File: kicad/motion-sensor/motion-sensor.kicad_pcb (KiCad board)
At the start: 2 copper layers, 53.7 x 28.7 mm, 0 parts

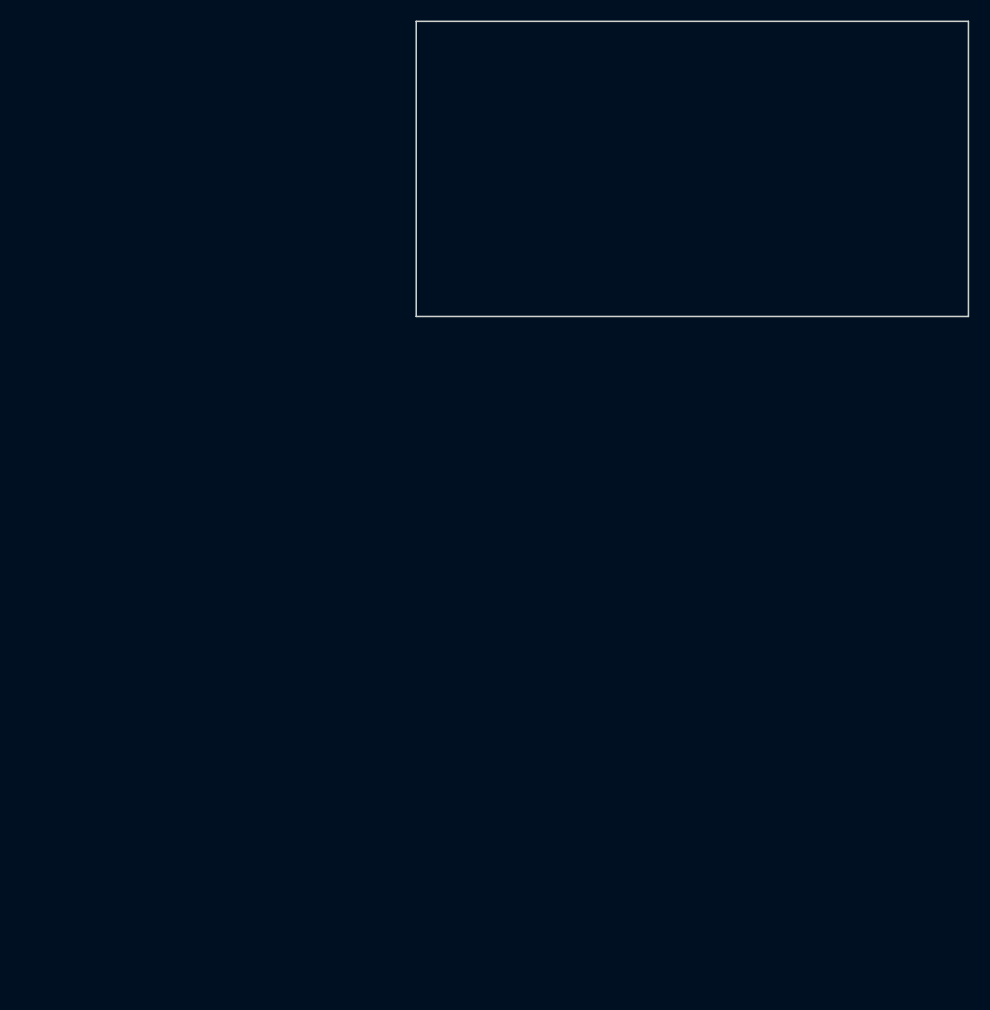
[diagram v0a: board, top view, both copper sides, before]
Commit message: motion sensor project in kicad
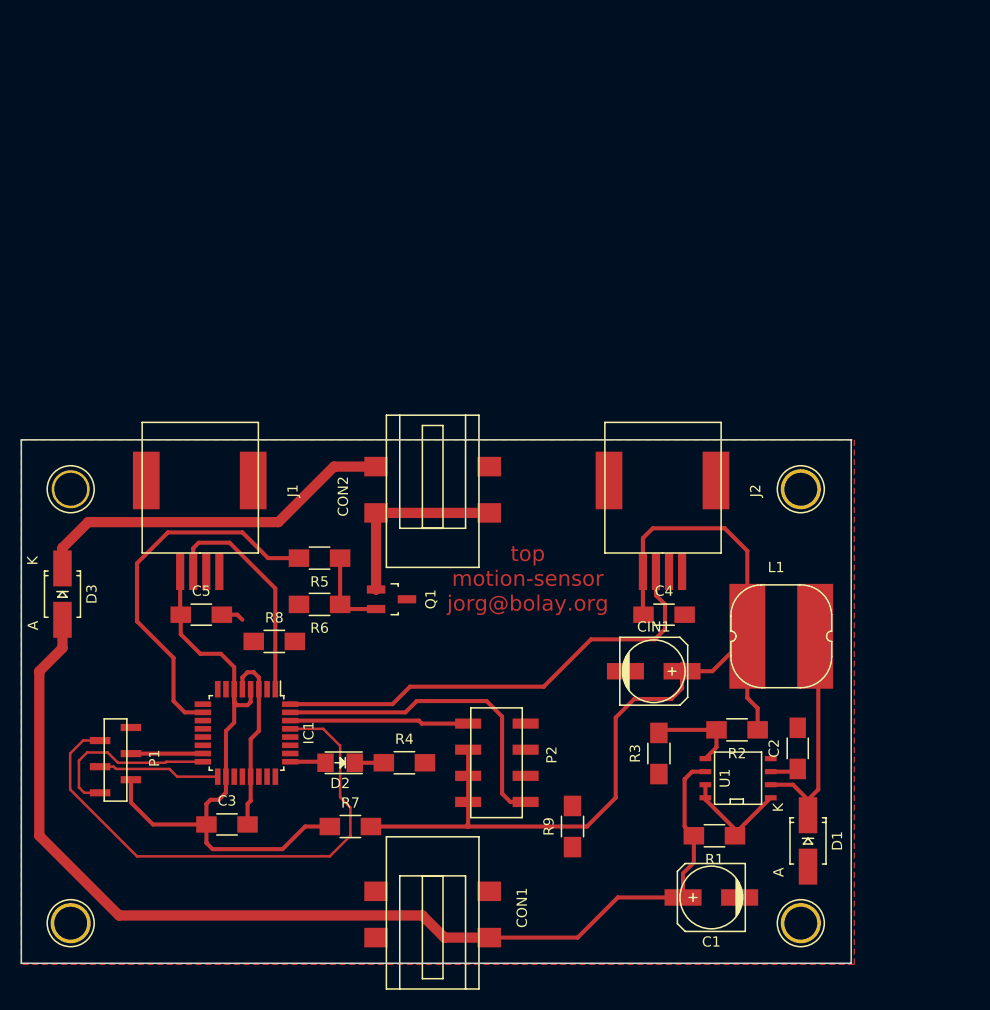
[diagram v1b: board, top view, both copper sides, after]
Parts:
- added C1: 100uF, Capacitors_SMD:c_elec_6.3x7.7, F.Cu at (117.1, 144.5)
- added C2: 160pF, Capacitors_SMD:C_1206_HandSoldering, F.Cu at (125.5, 130.0)
- added C3: 100nF, Capacitors_SMD:C_1206_HandSoldering, F.Cu at (70.0, 137.4)
- added C4: 100nF, Capacitors_SMD:C_1206_HandSoldering, F.Cu at (112.5, 117.0)
- added C5: 100nF, Capacitors_SMD:C_1206_HandSoldering, F.Cu at (67.5, 117.0)
- added CIN1: 50uF, Capacitors_SMD:c_elec_6.3x7.7, F.Cu at (111.5, 122.5)
- added CON1: LUM 1613-14, bolay library:barrel_jack_ds_1613_14, F.Cu at (90.0, 146.0)
- added CON2: LUM 1613-14, bolay library:barrel_jack_ds_1613_14, F.Cu at (90.0, 105.0)
- added D1: B140F, Diodes_SMD:SMA_Handsoldering, F.Cu at (126.5, 139.0)
- added D2: LED, LEDs:LED_1206, F.Cu at (81.0, 131.4)
- added D3: B140F, Diodes_SMD:SMA_Handsoldering, F.Cu at (54.0, 115.0)
- added IC1: ATMEGA328P-A AU 1537, Housings_QFP:TQFP-32_7x7mm_Pitch0.8mm, F.Cu at (71.9, 128.5)
- added J1: RJ10_4p4c, bolay library:RJ10_SMD_4p4c, F.Cu at (61.0, 111.0)
- added J2: RJ10_4p4c, bolay library:RJ10_SMD_4p4c, F.Cu at (106.0, 111.0)
- added L1: 35uH, bolay library:SRN_1060_Power_Inductors, F.Cu at (123.9, 119.1)
- added P1: ISP, bolay library:6x1pin_50mil_header, F.Cu at (59.4, 131.2)
- added P2: ESP8266, bolay library:8pin_Header_SMD, F.Cu at (96.5, 131.4)
- added Q1: FDN337N, TO_SOT_Packages_SMD:SOT-23_Handsoldering, F.Cu at (86.0, 115.5)
- added R1: 0.33, Resistors_SMD:R_1206_HandSoldering, F.Cu at (117.4, 138.5)
- added R2: 18k, Resistors_SMD:R_1206_HandSoldering, F.Cu at (119.6, 128.2)
- added R3: 11k, Resistors_SMD:R_1206_HandSoldering, F.Cu at (112.0, 130.5)
- added R4: 560, Resistors_SMD:R_1206_HandSoldering, F.Cu at (87.2, 131.4)
- added R5: 1K, Resistors_SMD:R_1206_HandSoldering, F.Cu at (79.0, 111.5)
- added R6: 1M, Resistors_SMD:R_1206_HandSoldering, F.Cu at (79.0, 116.0)
- added R7: 0, Resistors_SMD:R_1206_HandSoldering, F.Cu at (82.0, 137.6)
- added R8: 0, Resistors_SMD:R_1206_HandSoldering, F.Cu at (74.6, 119.6)
- added R9: 0, Resistors_SMD:R_1206_HandSoldering, F.Cu at (103.6, 137.6)
- added REF**: 1pin, Connect:1pin, F.Cu at (125.8, 104.8)
- added REF**: 1pin, Connect:1pin, F.Cu at (125.8, 147.0)
- added REF**: 1pin, Connect:1pin, F.Cu at (54.8, 104.8)
- added REF**: 1pin, Connect:1pin, F.Cu at (54.8, 147.0)
- added U1: MC34063, SMD_Packages:SOIC-8-N, F.Cu at (119.7, 132.9)
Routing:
- net +3V3: track 0.00 -> 157.0 mm
- net +12V: track 0.00 -> 104.9 mm
- net RESET: track 0.00 -> 52.4 mm
- net Motion_Sensor_Pin_2: track 0.00 -> 45.4 mm
- net PWM_Pin: track 0.00 -> 36.2 mm
- net Net-(CON2-Pad1): track 0.00 -> 35.8 mm
- net TXD: track 0.00 -> 33.0 mm
- net Net-(D1-Pad1): track 0.00 -> 24.1 mm
- net Motion_Sensor_Pin_1: track 0.00 -> 22.1 mm
- net GND: track 0.00 -> 20.8 mm
- net Net-(CON2-Pad2): track 0.00 -> 18.5 mm
- net RXD: track 0.00 -> 18.2 mm
- net MISO: track 0.00 -> 17.7 mm
- net SCK: track 0.00 -> 11.8 mm
- net Net-(R1-Pad1): track 0.00 -> 10.2 mm
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- added copper zone on F.Cu, net GND
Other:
- board size 53.7 x 28.7 mm -> 80.7 x 50.9 mm
- board text added: "top motion-sensor jorg@bolay.org"

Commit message: motion sensor Projekt für Küche und unter dem Bett
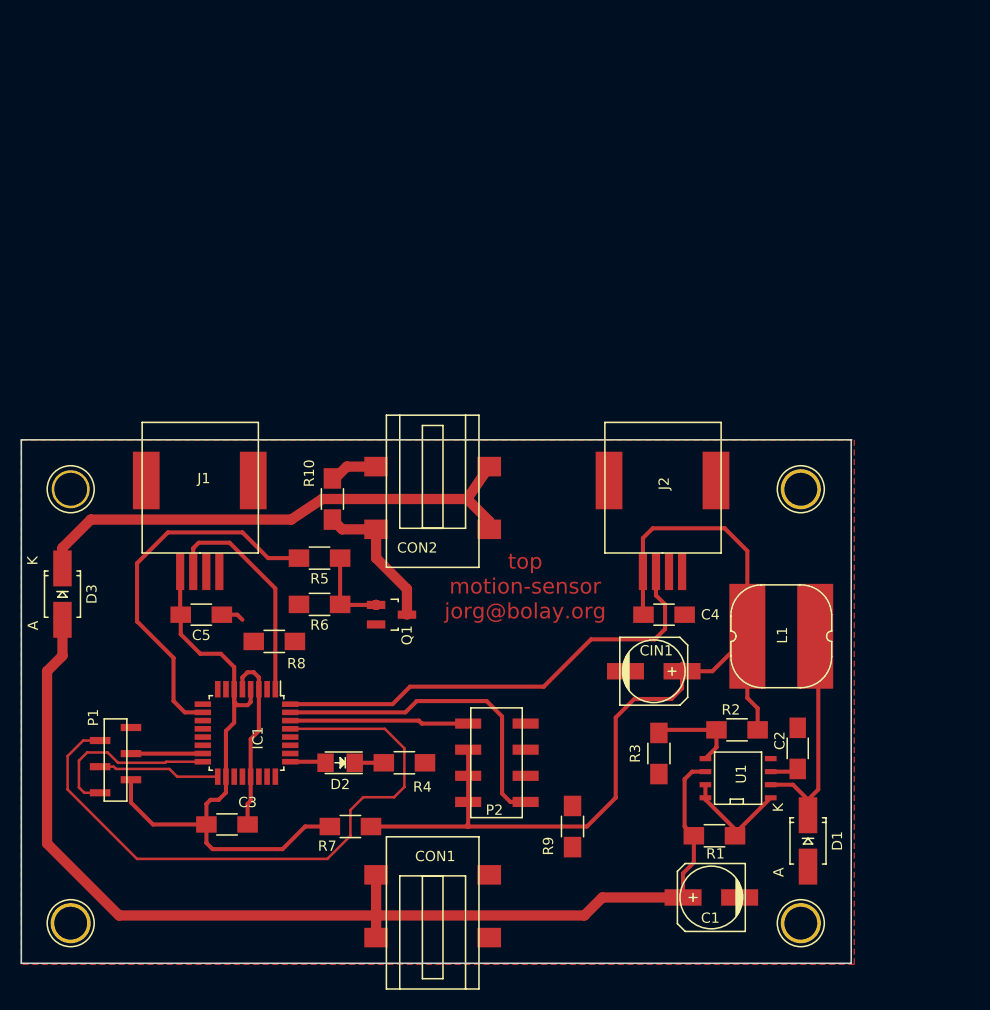
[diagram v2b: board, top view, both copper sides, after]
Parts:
- added R10: 0, Resistors_SMD:R_1206_HandSoldering, F.Cu at (80.2, 105.8)
- moved Q1 1.50 mm to (86.0, 117.0)
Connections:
- CON2 pad 3: Net-(CON2-Pad2) -> Net-(CON2-Pad3)
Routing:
- net Net-(CON2-Pad1): track 35.8 -> 50.7 mm
- net RESET: track 52.4 -> 62.6 mm
- net Net-(CON2-Pad3): track 0.00 -> 7.44 mm
- net Net-(CON2-Pad2): track 18.5 -> 11.5 mm
- net +12V: track 104.9 -> 109.1 mm
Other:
- board text added: "Blinkcodes 2x Blink -> Start 3x Blink -> eingelogt ins WLAN 1x kurz -> Daten senden 2x kurz -> Daten empfangen"
- board text added: "LED Strip"
- board text added: "Motion"
- board text added: "Power"
